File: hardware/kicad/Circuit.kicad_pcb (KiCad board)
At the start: 2 copper layers, 63 parts, among them IC1 AS312, J2 B2B-XH-A__LF__SN_, J3 Conn_01x08_Socket, J4 USB_C_Receptacle_USB2.0_14P, Q1 AO3400A, SW1 SW_Push, SW2 SW_Push, U1 BQ24075RGT, U2 TPS63070RNMR, U3 ESP32-C6-WROOM-1-N8, U4 BME680, Y1 32.768 kHz

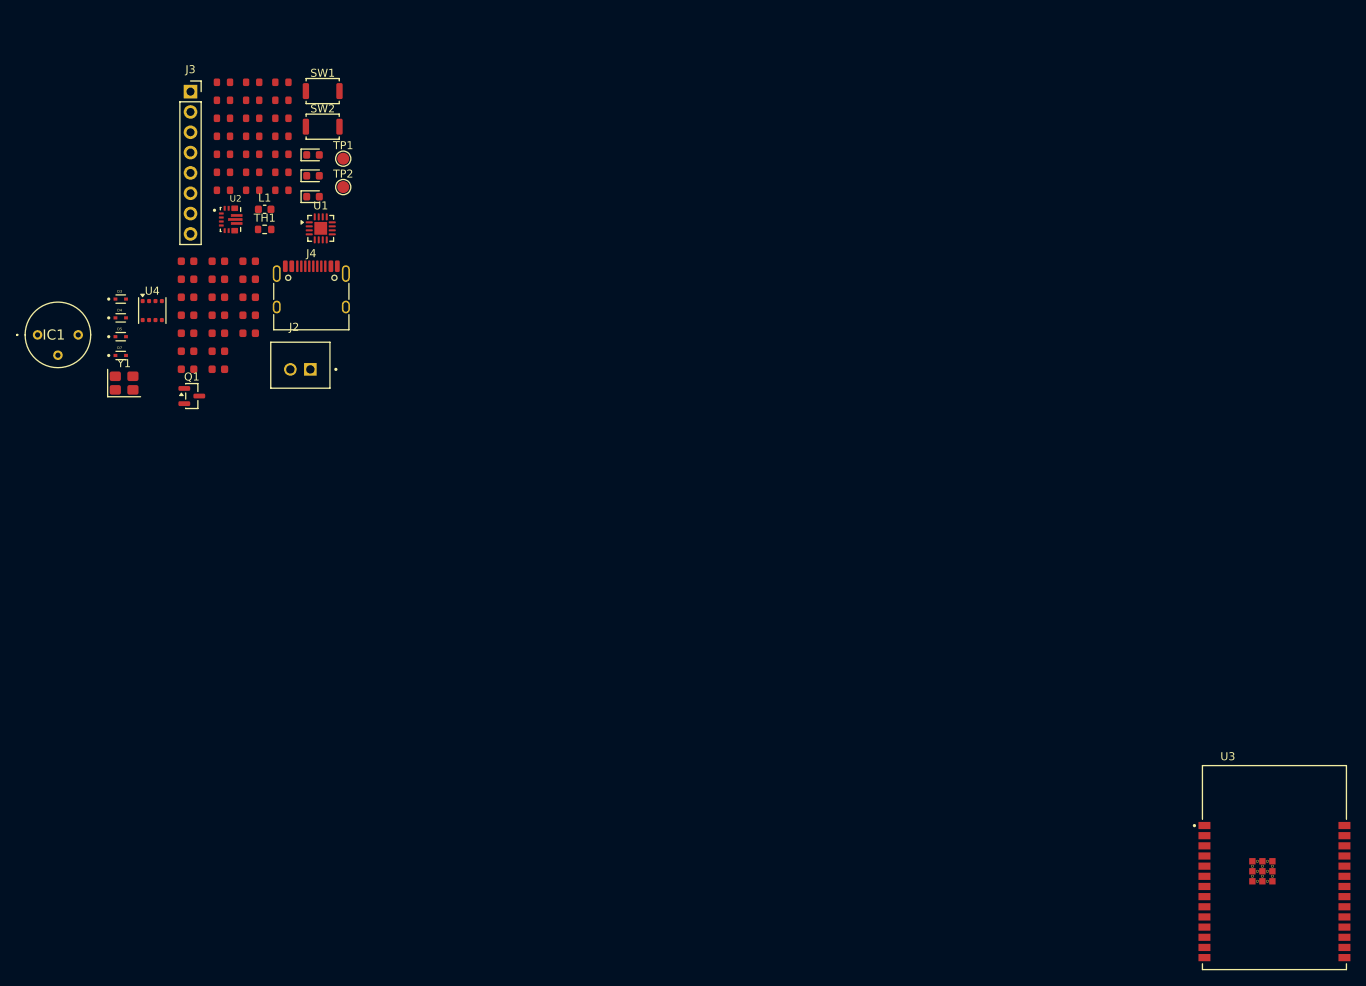
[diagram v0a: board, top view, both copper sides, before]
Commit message: hardware: ldr voltage divider
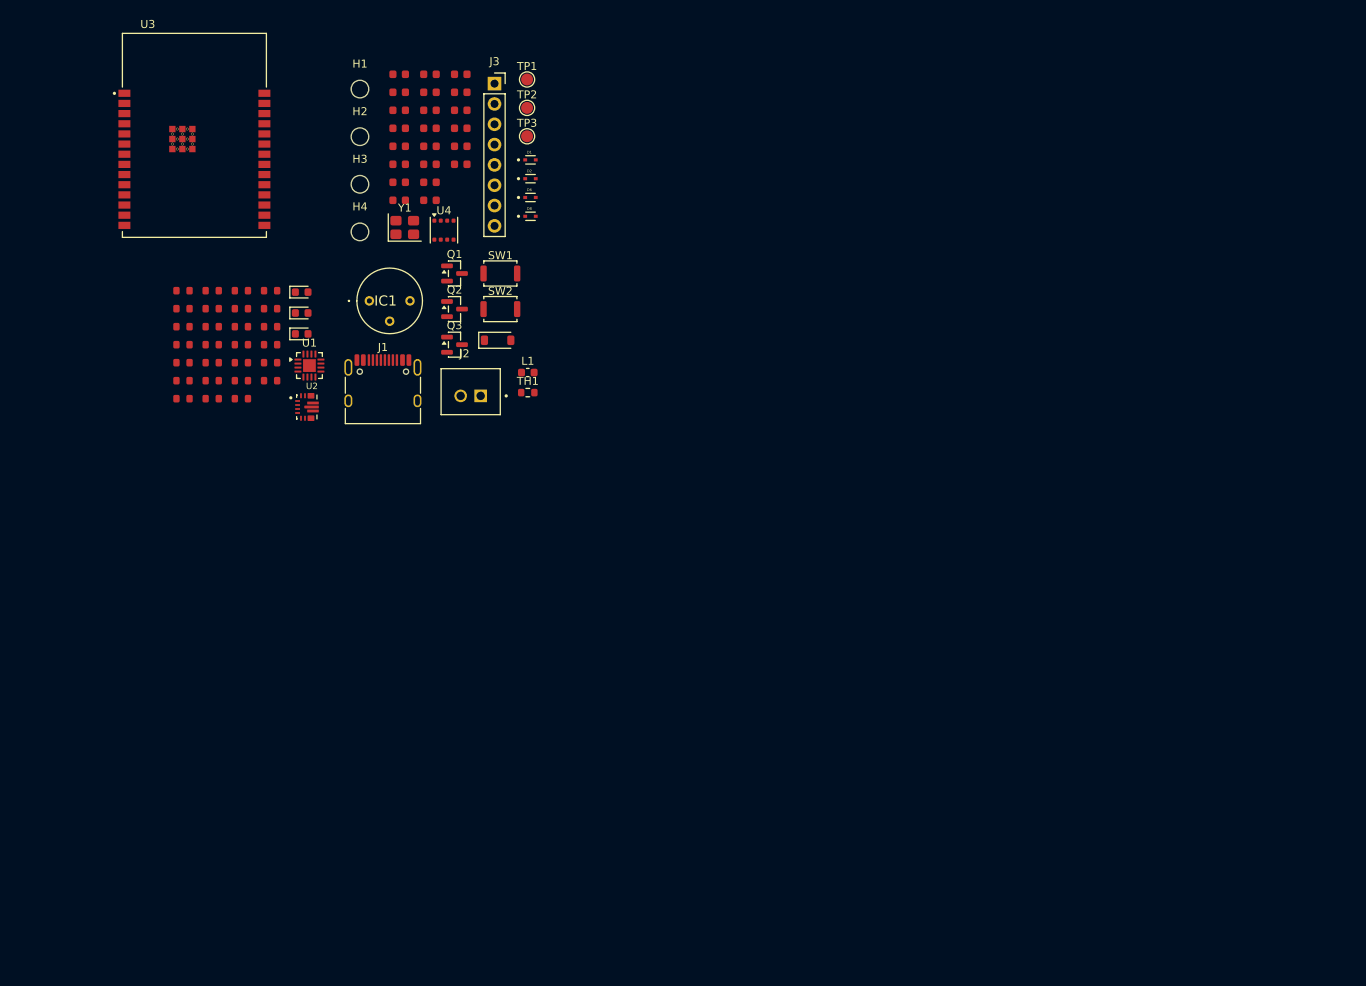
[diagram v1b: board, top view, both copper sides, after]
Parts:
- removed J4: USB_C_Receptacle_USB2.0_14P, Connector_USB:USB_C_Receptacle_HRO_TYPE-C-31-M-12
- added C20: 100nF, PCM_JLCPCB:C_0603, F.Cu at (16.5, 9.88)
- added C21: 12pF, PCM_JLCPCB:C_0603, F.Cu at (16.5, 12.1)
- added C22: 12pF, PCM_JLCPCB:C_0603, F.Cu at (16.5, 14.4)
- added D8: LESD5D5.0CT1G, Diode_SMD:TVS_LESD5D5.0CT1G, F.Cu at (25.3, 20.9)
- added H1: MountingHole, MountingHole:MountingHole_2.2mm_M2, F.Cu at (3.94, 4.97)
- added H2: MountingHole, MountingHole:MountingHole_2.2mm_M2, F.Cu at (3.94, 10.9)
- added H3: MountingHole, MountingHole:MountingHole_2.2mm_M2, F.Cu at (3.94, 16.9)
- added H4: MountingHole, MountingHole:MountingHole_2.2mm_M2, F.Cu at (3.94, 22.8)
- added J1: USB_C_Receptacle_USB2.0_14P, Connector_USB:USB_C_Receptacle_HRO_TYPE-C-31-M-12, F.Cu at (6.82, 42.9)
- added Q2: AO3401A, Package_TO_SOT_SMD:SOT-23, F.Cu at (15.8, 32.5)
- added Q3: AO3400A, Package_TO_SOT_SMD:SOT-23, F.Cu at (15.8, 36.9)
- added R22: 220, PCM_JLCPCB:R_0603, F.Cu at (-7.22, 30.2)
- added R23: 10K, PCM_JLCPCB:R_0603, F.Cu at (-7.22, 32.4)
- added R24: 4.7K, PCM_JLCPCB:R_0603, F.Cu at (-7.22, 34.7)
- added R25: 4.7K, PCM_JLCPCB:R_0603, F.Cu at (-7.22, 36.9)
- added R26: 4.7K, PCM_JLCPCB:R_0603, F.Cu at (-7.22, 39.2)
- added R27: 10M, PCM_JLCPCB:R_0603, F.Cu at (-7.22, 41.4)
- added TP3: TP_+3V3, TestPoint:TestPoint_Pad_D1.5mm, F.Cu at (24.8, 10.9)
- C10: value 12pF -> 100nF
- C11: value 12pF -> 22uF
- C12: value 10uF -> 100nF
- C13: value 100uF -> 100nF
- C14, C18: value 100nF -> 1uF
- C15: value 1uF -> 10uF
- C16: value 22uF -> 100nF
- C4: value 10uF -> 4.7uF
- C6: value 100nF -> 10uF
- C8: value 22uF -> 10uF
- C9: value 10uF -> 1uF
- D1: value Green -> LESD5D5.0CT1G; footprint PCM_JLCPCB:D_0603 -> Diode_SMD:TVS_LESD5D5.0CT1G
- D2: value Red -> LESD5D5.0CT1G; footprint PCM_JLCPCB:D_0603 -> Diode_SMD:TVS_LESD5D5.0CT1G
- D3: value LESD5D5.0CT1G -> Green; footprint Diode_SMD:TVS_LESD5D5.0CT1G -> PCM_JLCPCB:D_0603
- D4: value LESD5D5.0CT1G -> Red; footprint Diode_SMD:TVS_LESD5D5.0CT1G -> PCM_JLCPCB:D_0603
- D5: value LESD5D5.0CT1G -> BZT52C6V2; footprint Diode_SMD:TVS_LESD5D5.0CT1G -> PCM_JLCPCB:D_SOD-123
- D6: value Blue -> LESD5D5.0CT1G; footprint PCM_JLCPCB:D_0603 -> Diode_SMD:TVS_LESD5D5.0CT1G
- D7: value LESD5D5.0CT1G -> Blue; footprint Diode_SMD:TVS_LESD5D5.0CT1G -> PCM_JLCPCB:D_0603
- Q1: value AO3400A -> AO3401A
- R1: value 1.1K -> 37.5K
- R11: value 10M -> 100K
- R12: value 10K -> 100K
- R13: value 1K -> 10K
- R14: value 1K -> 470K
- R15: value 330 -> 150K
- R16: value 220 -> 100K
- R17: value 10K -> 1K
- R18, R20: value 4.7K -> 10K
- R2: value 887 -> 1.1K
- R21: value 4.7K -> 330
- R3: value 5k1 -> 887
- R4, R5: value 1.5K -> 5k1
- R6: value 5k1 -> 100K
- R7: value 10K -> 1.5K
- R8: value 470K -> 1.5K
- R9: value 150K -> 100K
- TP2: value TP_+3V3 -> TP_VBUS
- moved U3 163.1 mm to (-16.8, 10.8)
- moved D5 47.1 mm to (21.2, 36.4)
- moved IC1 41.7 mm to (5.12, 31.4)
- moved Y1 40.1 mm to (9.54, 22.3)
- moved L1 38.7 mm to (24.9, 40.4)
- moved TH1 38.7 mm to (24.9, 42.9)
- moved C18 38.4 mm to (16.5, 5.38)
- moved C19 38.4 mm to (16.5, 7.62)
- moved C17 38.4 mm to (16.5, 3.12)
- moved J3 38.0 mm to (20.8, 4.29)
- moved U4 37.8 mm to (14.4, 22.6)
- moved C10 36.8 mm to (12.7, 5.38)
- moved C11 36.8 mm to (12.7, 7.62)
- moved C12 36.8 mm to (12.7, 9.88)
- moved C13 36.8 mm to (12.7, 12.1)
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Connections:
- net IO9 renamed Net-(U3-IO9)
- net TS renamed Net-(U1-TS)
- C10 pad 2: XTAL_P -> BAT_ADC
- C11 pad 1: GND -> +3.3V
- C11 pad 2: XTAL_N -> GND
- C12 pad 1: +3.3V -> Net-(U2-VAUX)
- C14 pad 1: GND -> Net-(U3-EN)
- C14 pad 2: +3.3V -> GND
- C15 pad 1: Net-(U3-EN) -> GND
- C15 pad 2: GND -> +3.3V
- C16 pad 1: +3.3V -> GND
- C16 pad 2: GND -> +3.3V
- C17 pad 1: +3.3V -> GND
- C17 pad 2: GND -> +3.3V
- C4 pad 1: GND -> Net-(C4-Pad1)
- C4 pad 2: +5V -> GND
- C5 pad 1: +3.3V -> GND
- C5 pad 2: GND -> +5V
- C6 pad 1: Net-(U2-VAUX) -> DPM_OUT
- C7 pad 1: DPM_OUT -> +3.3V
- C8 pad 1: +3.3V -> DPM_OUT
- C9 pad 1: DPM_OUT -> GND
- C9 pad 2: GND -> BAT_ADC
- D1 pad 1: Net-(D1-Pad1) -> GND
- D1 pad 2: DPM_OUT -> D-
- D2 pad 1: Net-(D2-Pad1) -> GND
- D2 pad 2: DPM_OUT -> D+
- D3 pad 1: GND -> Net-(D3-Pad1)
- D3 pad 2: +5V -> DPM_OUT
- D4 pad 1: GND -> Net-(D4-Pad1)
- D4 pad 2: D- -> DPM_OUT
- D5 pad 1: GND -> +5V
- D5 pad 2: D+ -> Net-(Q1-G)
- D6 pad 1: IO18 -> GND
- D6 pad 2: Net-(D6-Pad2) -> +5V
- D7 pad 1: GND -> Net-(U3-IO18)
- D7 pad 2: +3.3V -> Net-(D7-Pad2)
- IC1 pad 2: PIR -> Net-(IC1-REL)
- Q1 pad 2: GND -> +5V
- Q1 pad 3: BL -> Net-(Q1-D)
- R1 pad 2: Net-(U1-ILIM) -> Net-(U1-TMR)
- R10 pad 1: +3.3V -> BAT_ADC
- R10 pad 2: PG -> GND
- R11 pad 1: XTAL_P -> BAT
- R11 pad 2: XTAL_N -> Net-(Q2-G)
- R12 pad 1: PIR -> BAT_CTRL
- R12 pad 2: GND -> Net-(Q2-G)
- R13 pad 1: +3.3V -> DPM_OUT
- R13 pad 2: IO8 -> Net-(U2-EN)
- R14 pad 2: Net-(U3-EN) -> FB
- R15 pad 1: +3.3V -> FB
- R15 pad 2: Net-(D6-Pad2) -> GND
- R16 pad 1: PWM -> +3.3V
- R16 pad 2: Net-(Q1-G) -> PG
- R17 pad 1: GND -> +3.3V
- R17 pad 2: Net-(Q1-G) -> Net-(U3-IO8)
- R18 pad 1: BL -> PIR
- R18 pad 2: +3.3V -> Net-(IC1-REL)
- R19 pad 1: Net-(U3-IO19) -> Net-(IC1-REL)
- R19 pad 2: PIR -> GND
- R2 pad 2: Net-(U1-ISET) -> Net-(U1-ILIM)
- R20 pad 2: S_SDA -> Net-(U3-EN)
- R21 pad 2: S_SCL -> Net-(D7-Pad2)
- R3 pad 1: CC1 -> GND
- R3 pad 2: GND -> Net-(U1-ISET)
- R4 pad 1: Net-(D1-Pad1) -> Net-(J1-CC2)
- R4 pad 2: ~{PGOOD} -> GND
- R5 pad 1: Net-(D2-Pad1) -> Net-(J1-CC1)
- R5 pad 2: ~{CHG} -> GND
- R6 pad 1: CC2 -> Net-(Q1-G)
- R7 pad 1: DPM_OUT -> Net-(D3-Pad1)
- R7 pad 2: Net-(U2-EN) -> ~{PGOOD}
- R8 pad 1: +3.3V -> Net-(D4-Pad1)
- R8 pad 2: FB -> ~{CHG}
- R9 pad 1: FB -> Net-(Q2-D)
- R9 pad 2: GND -> BAT_ADC
- TP1 pad 1: +5V -> DPM_OUT
- TP2 pad 1: +3.3V -> +5V
- U1 pad 14: GND -> Net-(U1-TMR)
- U1 pad 2: BAT -> Net-(C4-Pad1)
- U1 pad 3: BAT -> Net-(C4-Pad1)
- U3 pad 10: IO8 -> Net-(U3-IO8)
- U3 pad 12: unconnected-(U3-IO11-Pad12) -> BAT_CTRL
- U3 pad 16: IO18 -> Net-(U3-IO18)
- U3 pad 17: Net-(U3-IO19) -> PIR
- U3 pad 26: unconnected-(U3-IO3-Pad26) -> BAT_ADC

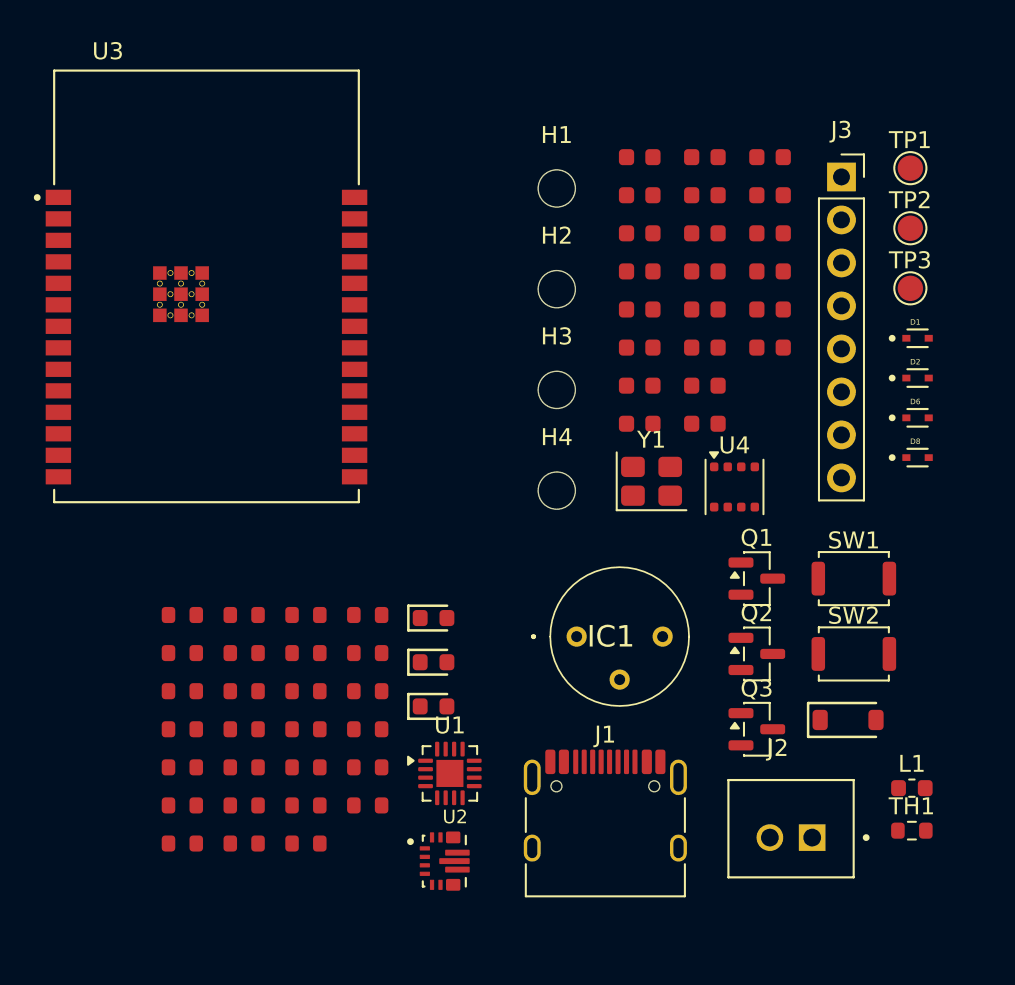
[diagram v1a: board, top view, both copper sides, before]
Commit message: feat: manufacturer part numbers
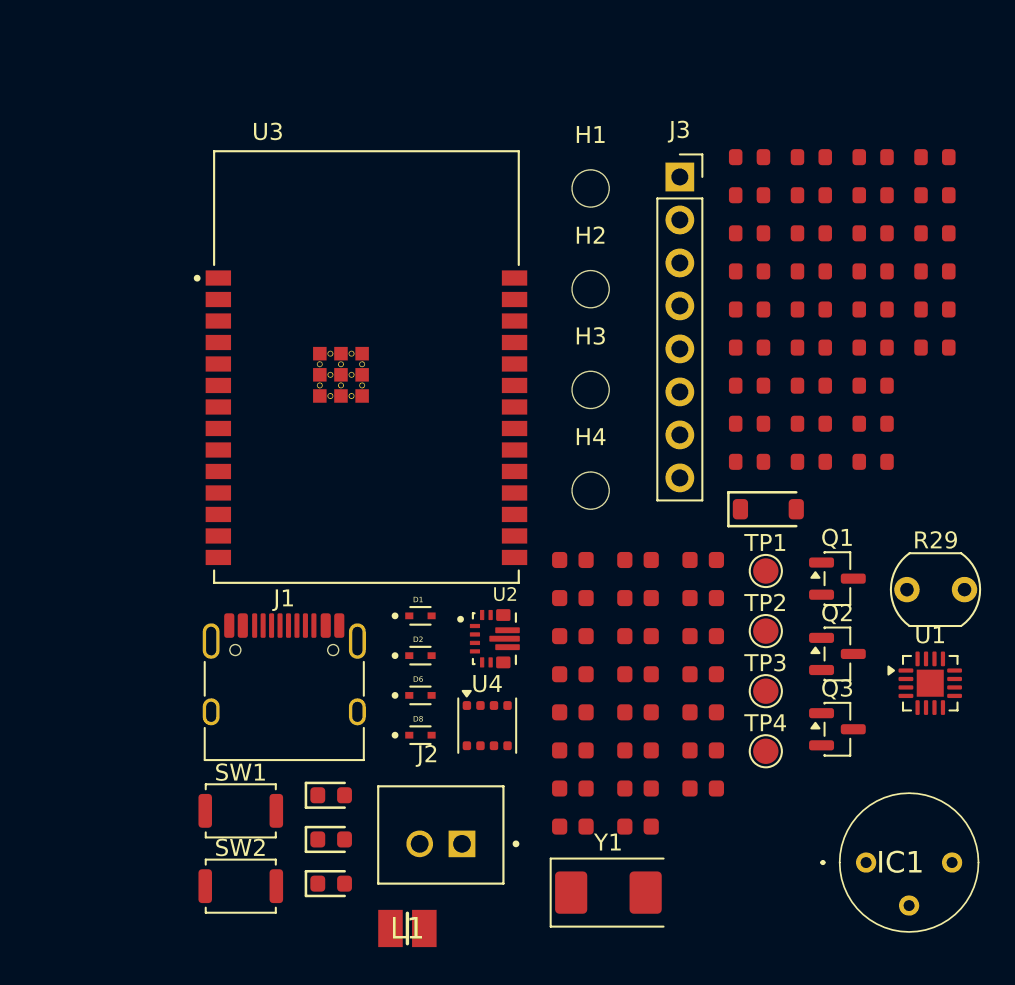
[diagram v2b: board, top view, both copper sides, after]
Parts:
- added C23: 100nF, PCM_JLCPCB:C_0603, F.Cu at (12.6, 40.4)
- added R28: 4.7K, PCM_JLCPCB:R_0603, F.Cu at (26.3, 3.12)
- added R29: R_Photo, OptoDevice:R_LDR_5.1x4.3mm_P3.4mm_Vertical, F.Cu at (24.6, 28.7)
- added R30: 30K, PCM_JLCPCB:R_0603, F.Cu at (26.3, 5.38)
- added R31: 4.7K, PCM_JLCPCB:R_0603, F.Cu at (26.3, 7.62)
- added R32: 4.7K, PCM_JLCPCB:R_0603, F.Cu at (26.3, 9.88)
- added R33: 10M, PCM_JLCPCB:R_0603, F.Cu at (26.3, 12.1)
- added TP4: TP_+3V3, TestPoint:TestPoint_Pad_D1.5mm, F.Cu at (16.3, 38.2)
- C10, C19: value 100nF -> 1uF
- C11: value 22uF -> 100nF
- C12: value 100nF -> 22uF
- C14, C18: value 1uF -> 100nF
- C15: value 10uF -> 1uF
- C16: value 100nF -> 10uF
- C4: value 4.7uF -> 2.2uF
- C5: value 10uF -> 4.7uF
- C6: value 10uF -> 2.2uF
- C9: value 1uF -> 10uF
- L1: value 1.5uH -> 1.5uH 4A; footprint Inductor_SMD:L_0603_1608Metric -> AOTA-B252010S1R5MT:INDC2520X100N
- R1: value 37.5K -> 75K
- R2: value 1.1K -> 1.6K
- R21: value 330 -> 100K
- R22: value 220 -> 100K
- R23: value 10K -> 220
- R24: value 4.7K -> 10K
- R25, R26: value 4.7K -> 100K
- R27: value 10M -> 330
- R3: value 887 -> 1.78K
- R6: value 100K -> 470K
- TH1: footprint Resistor_SMD:R_0603_1608Metric -> PCM_JLCPCB:R_0603
- TP1: value TP_VBUS -> TP_SYS
- Y1: footprint Crystal:Crystal_SMD_3225-4Pin_3.2x2.5mm -> Crystal:Crystal_SMD_0603-2Pin_6.0x3.5mm
- moved R19 49.2 mm to (22.6, 3.12)
- moved R20 49.2 mm to (22.6, 5.38)
- moved R21 49.2 mm to (22.6, 7.62)
- moved R10 46.0 mm to (19.0, 3.12)
- moved R11 46.0 mm to (19.0, 5.38)
- moved R12 46.0 mm to (19.0, 7.62)
- moved R13 46.0 mm to (19.0, 9.88)
- moved R14 46.0 mm to (19.0, 12.1)
- moved R1 43.1 mm to (15.3, 3.12)
- moved R2 43.1 mm to (15.3, 5.38)
- moved R3 43.1 mm to (15.3, 7.62)
- moved R4 43.1 mm to (15.3, 9.88)
- moved R5 43.1 mm to (15.3, 12.1)
- moved R6 43.1 mm to (15.3, 14.4)
- moved R7 43.1 mm to (15.3, 16.6)
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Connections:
- C11 pad 1: +3.3V -> GND
- C11 pad 2: GND -> BAT_ADC
- C12 pad 1: Net-(U2-VAUX) -> +3.3V
- C13 pad 1: Net-(U3-EN) -> Net-(U2-VAUX)
- C15 pad 1: GND -> Net-(U3-EN)
- C15 pad 2: +3.3V -> GND
- C18 pad 1: +3.3V -> GND
- C18 pad 2: GND -> +3.3V
- C4 pad 1: Net-(C4-Pad1) -> GND
- C4 pad 2: GND -> Net-(Q1-G)
- C5 pad 1: GND -> BAT
- C5 pad 2: +5V -> GND
- C6 pad 1: DPM_OUT -> GND
- C6 pad 2: GND -> +5V
- C7 pad 1: +3.3V -> DPM_OUT
- C8 pad 1: DPM_OUT -> +3.3V
- C9 pad 1: GND -> DPM_OUT
- C9 pad 2: BAT_ADC -> GND
- R2 pad 1: GND -> Net-(U1-SYSOFF)
- R21 pad 1: +3.3V -> CHG_EN1
- R21 pad 2: Net-(D7-Pad2) -> GND
- R22 pad 1: PWM -> CHG_EN2
- R22 pad 2: Net-(Q3-G) -> GND
- R23 pad 1: GND -> PWM
- R24 pad 1: BL -> GND
- R24 pad 2: +3.3V -> Net-(Q3-G)
- R25 pad 1: +3.3V -> +5V
- R25 pad 2: S_SDA -> VBUS_SENSE
- R26 pad 1: +3.3V -> VBUS_SENSE
- R26 pad 2: S_SCL -> GND
- R27 pad 1: XTAL_P -> +3.3V
- R27 pad 2: XTAL_N -> Net-(D7-Pad2)
- R3 pad 1: GND -> Net-(U1-SYSOFF)
- U1 pad 15: GND -> Net-(U1-SYSOFF)
- U1 pad 2: Net-(C4-Pad1) -> BAT
- U1 pad 3: Net-(C4-Pad1) -> BAT
- U1 pad 4: GND -> Net-(U1-SYSOFF)
- U1 pad 5: +5V -> CHG_EN2
- U1 pad 6: GND -> CHG_EN1
- U3 pad 24: unconnected-(U3-RXD0/GPIO17-Pad24) -> CHG_EN2
- U3 pad 27: unconnected-(U3-IO2-Pad27) -> CHG_EN1
- U3 pad 4: unconnected-(U3-IO4-Pad4) -> LDR
- U3 pad 5: unconnected-(U3-IO5-Pad5) -> VBUS_SENSE
